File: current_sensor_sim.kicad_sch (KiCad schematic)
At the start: 7 parts

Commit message: built opamp network
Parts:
- added C10, C8: 100p, symbol Device:C
- added C7, C9: 1u, symbol Device:C
- added I4: ISIN, Package_QFP:TQFP-44_10x10mm_P0.8mm, symbol Simulation_SPICE:ISIN
- added R10, R17: 100k, symbol Device:R
- added R11, R12, R13, R15, R16, R9: 10k, symbol Device:R
- added R28: 50k, symbol Device:R
- added R8: 100, symbol Device:R
- added U2, U3: ${SIM.PARAMS}, symbol Simulation_SPICE:OPAMP
- added V3: 5, Package_QFP:TQFP-44_10x10mm_P0.8mm, symbol Simulation_SPICE:VDC
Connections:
- net GND: now also C8.2, R10.2, R12.2, R16.2, R28.1, U2.4 (V-), U2.5, U3.3 (V+), V3.2
- new net: I4.2, R11.2, R12.1, R8.2, U2.2 (-)
- new net: C7.1, I4.1, R8.1
- new net: C7.2, R9.1
- new net: C8.1, R10.1, R9.2, U2.1 (+)
- new net: C10.1, R15.2, R17.1, U3.2 (-)
- new net: C9.1, R28.2
- new net: R13.2, R16.1, U3.1 (+)
- new net: C9.2, R15.1
- new net +5V: R11.1, R13.1, U2.3 (V+), U3.4 (V-), V3.1
- new net I_{sns}: C10.2, R17.2, U3.5
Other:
- note added: ".tran 5u 200m 50m 10u"
- note removed: ".tran 1u 200m 50m 10u"

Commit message: opamp chain fix
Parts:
- removed R28: 50k, symbol Device:R
- C7, C9: value 1u -> 1n
- R10: value 100k -> 10k
- R17: value 100k -> 5k
- R8: value 100 -> 50
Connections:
- net +5V: now also U3.3 (V+); no longer U3.4 (V-)
- net GND: now also C7.2, C9.2, U3.4 (V-); no longer C8.2, R10.2, U2.5, U3.3 (V+)
- net at I4.2, R11.2, R12.1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: now also U2.1 (+); no longer U2.2 (-)
- net at C7.1, I4.1, R8.1: now also R9.1
- net at C8.1, R10.1, R9.2: now also U2.2 (-); no longer U2.1 (+)
- net I_{snspre}: now reaches C9.1
- net I_{snspre}: now also C8.2, R10.2, R15.1, U2.5
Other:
- note added: ".tran 10u 200m 50m"
- note removed: ".tran 5u 200m 50m 10u"
- moved on the sheet: C7, C9

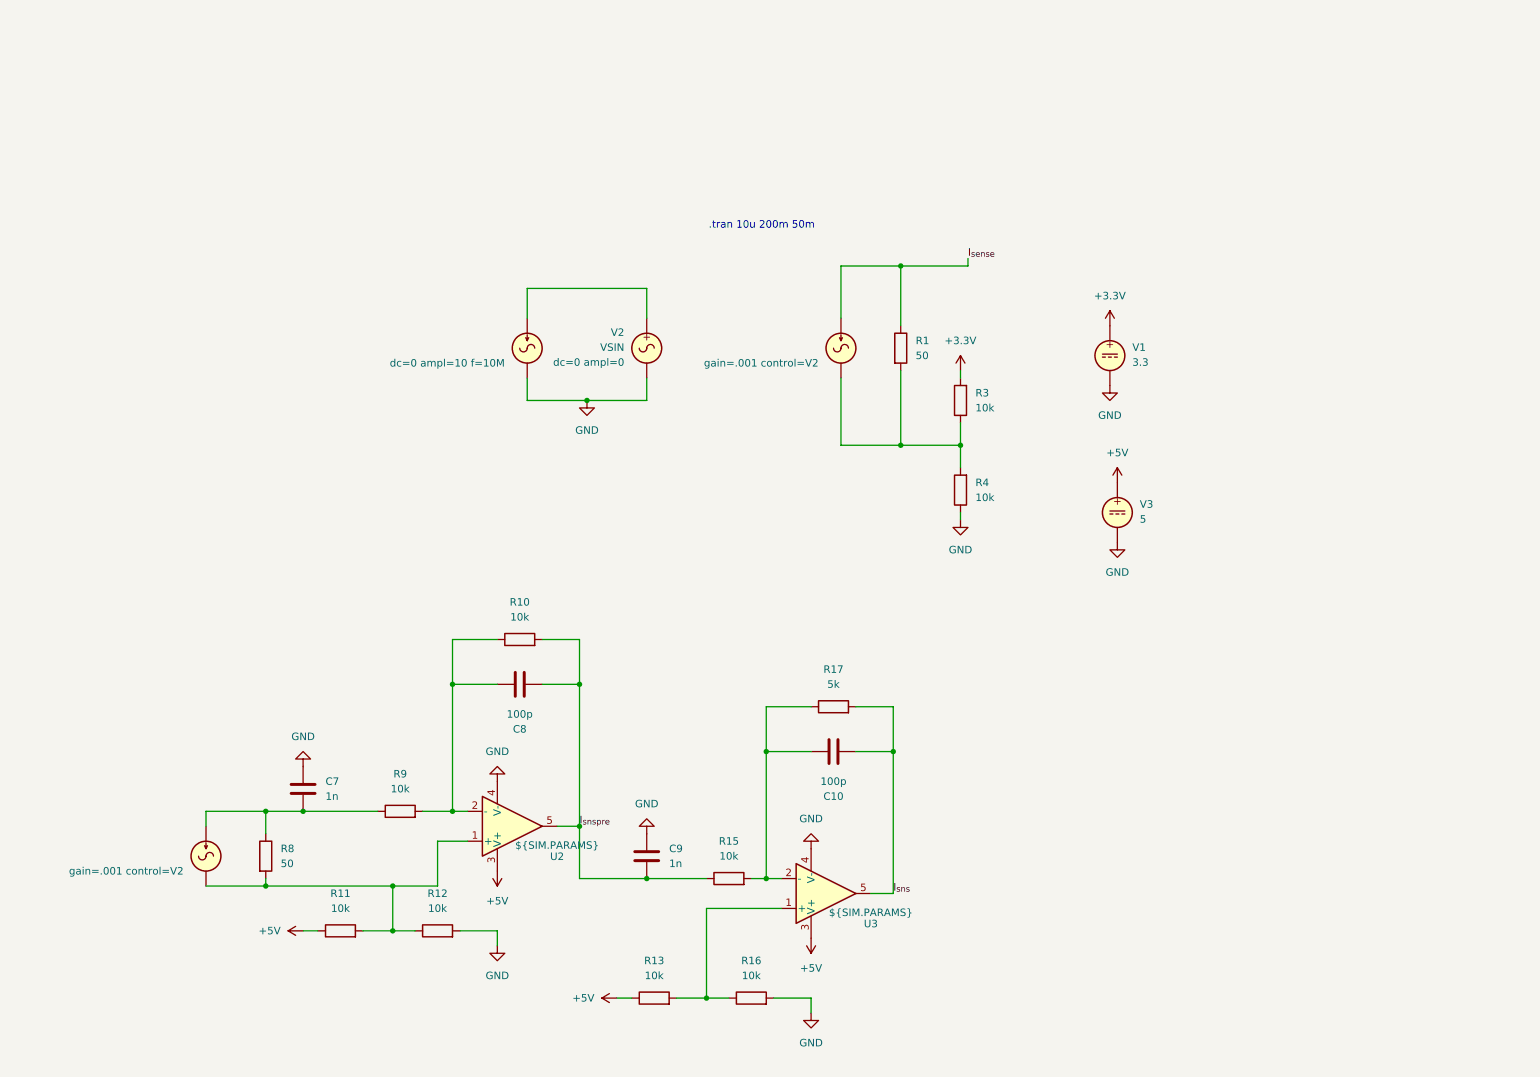
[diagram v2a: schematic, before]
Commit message: add rectifier simulation
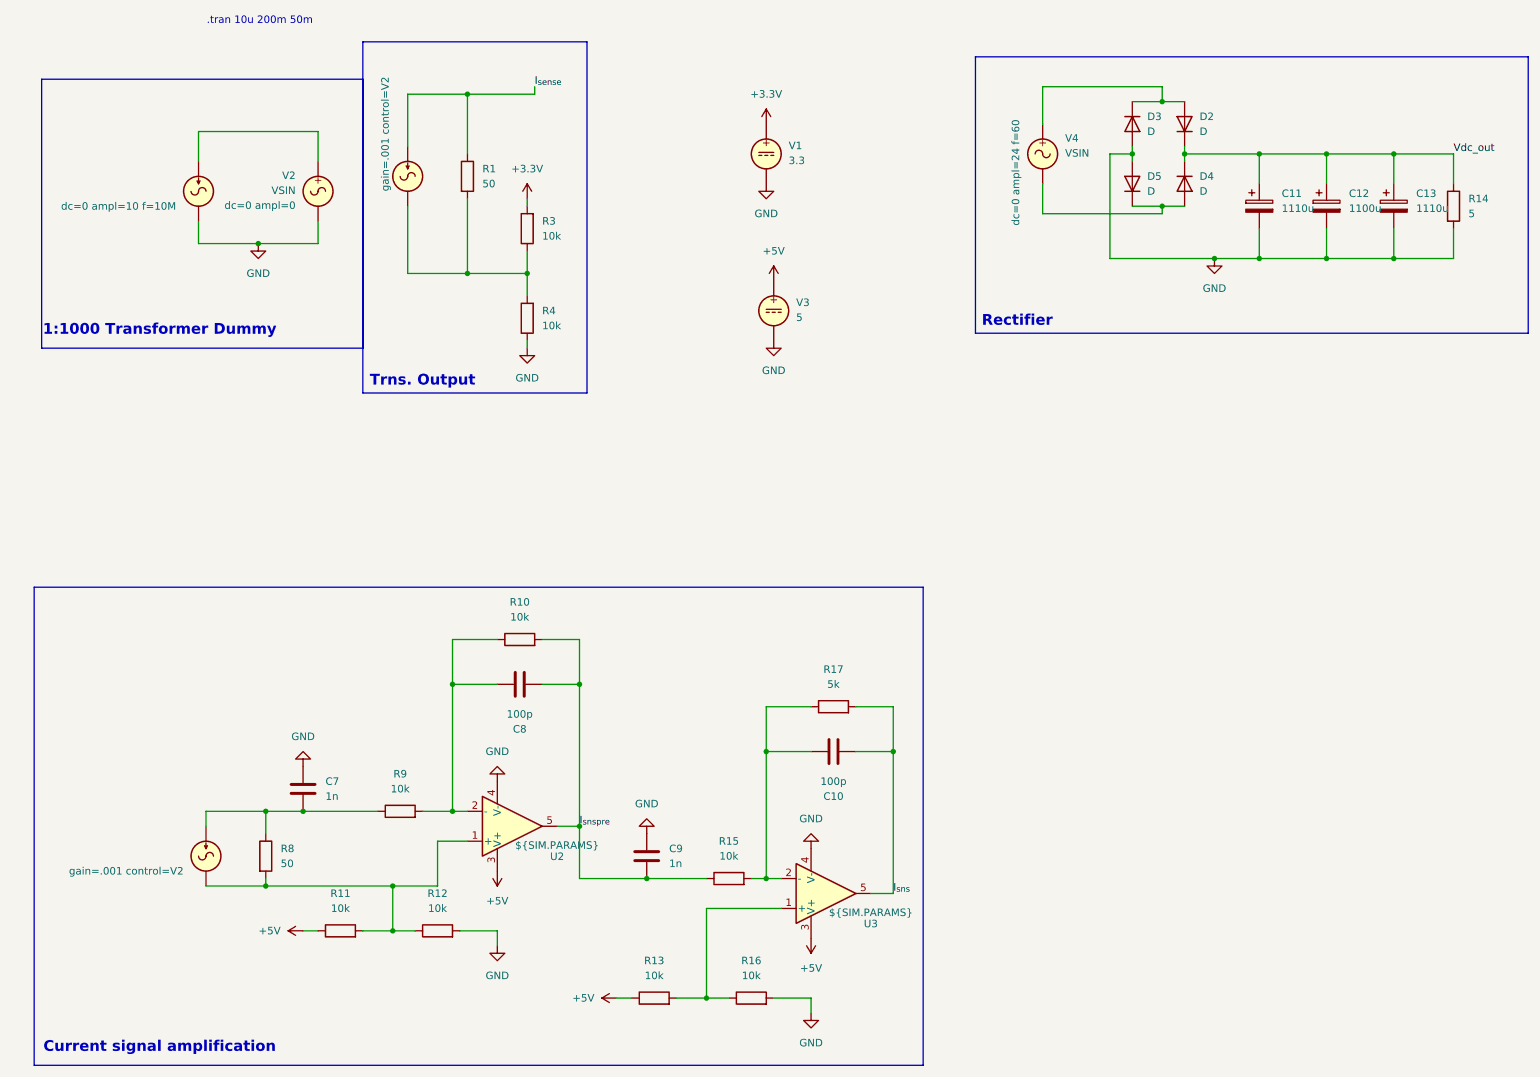
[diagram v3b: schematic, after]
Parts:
- added C11, C13: 1110u, Package_DIP:DIP-24_W7.62mm, symbol Device:C_Polarized
- added C12: 1100u, Package_DIP:DIP-24_W7.62mm, symbol Device:C_Polarized
- added D2, D3, D4, D5: D, symbol Device:D
- added R14: 5, symbol Device:R
- added V4: VSIN, Package_QFP:TQFP-44_10x10mm_P0.8mm, symbol Simulation_SPICE:VSIN
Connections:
- net GND: now also C11.2, C12.2, C13.2, D3.2 (A), D5.2 (A), R14.2
- new net: D2.2 (A), D3.1 (K), V4.1
- new net: D4.2 (A), D5.1 (K), V4.2
- new net Vdc_out: C11.1, C12.1, C13.1, D2.1 (K), D4.1 (K), R14.1
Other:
- note added: "1:1000 Transformer Dummy"
- note added: "Current signal amplification"
- note added: "Rectifier"
- note added: "Trns. Output"
- moved on the sheet: R1, R3, R4, V1, V2, V3

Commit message: ade7953 breakout board
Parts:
- removed C11, C13: 1110u, Package_DIP:DIP-24_W7.62mm, symbol Device:C_Polarized
- removed C12: 1100u, Package_DIP:DIP-24_W7.62mm, symbol Device:C_Polarized
- removed D2, D3, D4, D5: D, symbol Device:D
- removed I2: ISIN, Package_QFP:TQFP-44_10x10mm_P0.8mm, symbol Simulation_SPICE:ISIN
- removed R1: 50, symbol Device:R
- removed R14: 5, symbol Device:R
- removed R3, R4: 10k, symbol Device:R
- removed V1: 3.3, Package_QFP:TQFP-44_10x10mm_P0.8mm, symbol Simulation_SPICE:VDC
- removed V3: 5, Package_QFP:TQFP-44_10x10mm_P0.8mm, symbol Simulation_SPICE:VDC
- removed V4: VSIN, Package_QFP:TQFP-44_10x10mm_P0.8mm, symbol Simulation_SPICE:VSIN
- renumbered I3 to I1, I4 to I2, R8 to R1, R15 to R14, R16 to R15, R17 to R16, R11 to R3, R9 to R4, R12 to R8, V2 to V1
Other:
- note removed: ".tran 10u 200m 50m"
- note removed: "Rectifier"
- note removed: "Trns. Output"
- moved on the sheet: V1
